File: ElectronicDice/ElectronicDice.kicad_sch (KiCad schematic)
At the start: 17 parts, among them J1 Conn_01x02_Pin, SW1 SW_Push

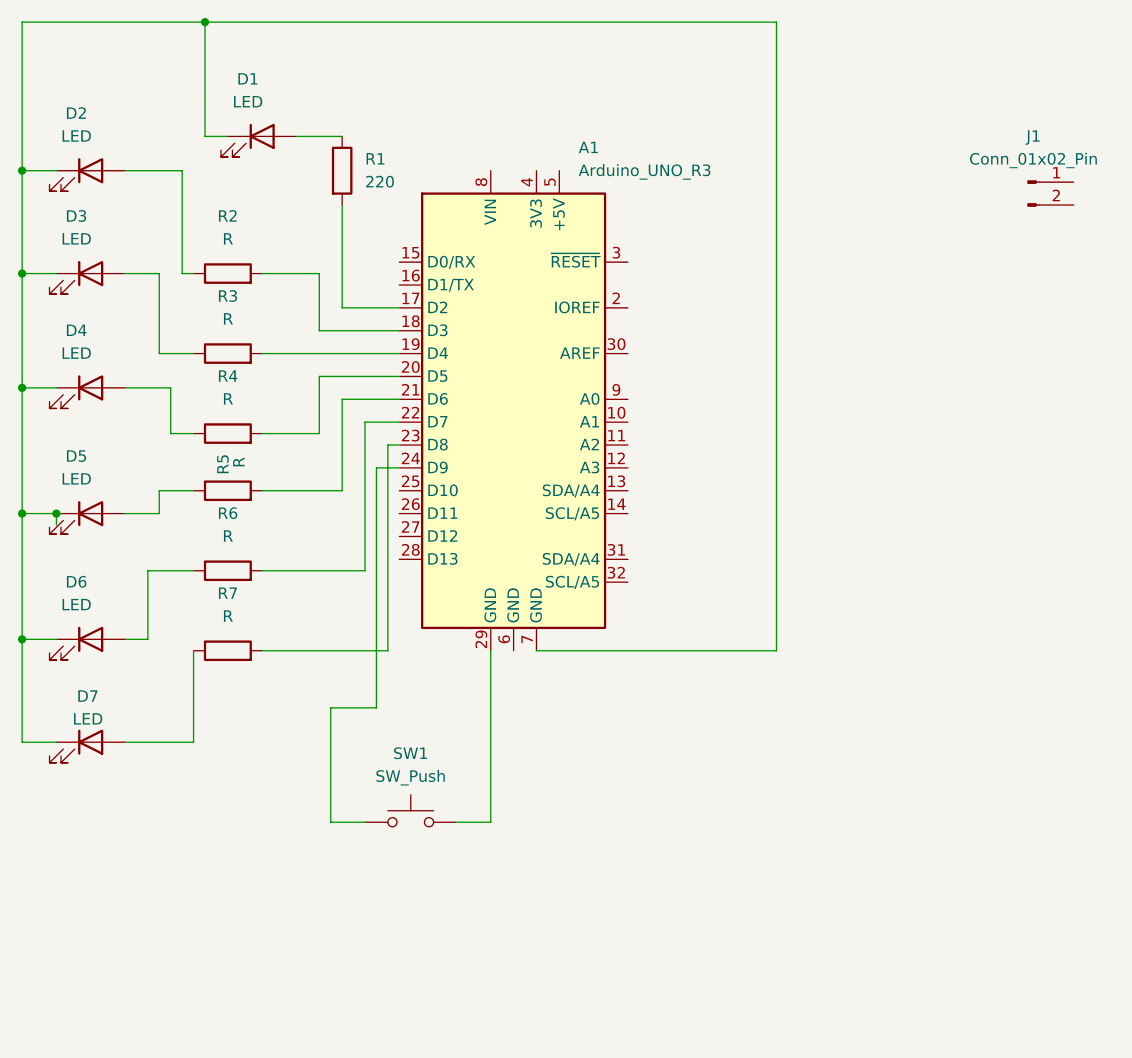
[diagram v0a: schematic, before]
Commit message: Assigned Footprints
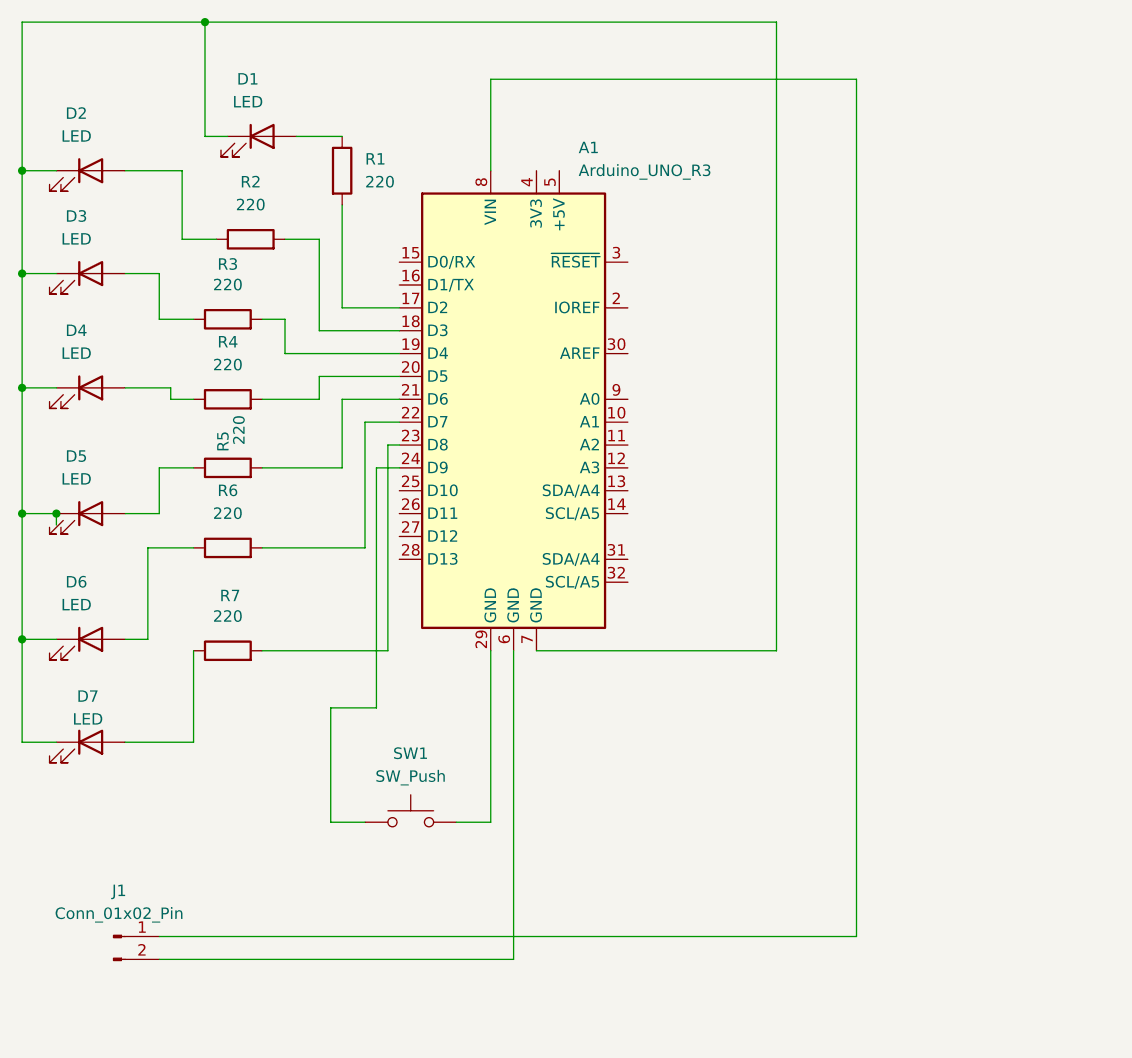
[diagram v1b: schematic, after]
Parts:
- D1, D2, D3, D4, D5, D6, D7: footprint (none) -> LED_THT:LED_D5.0mm
- J1: footprint (none) -> Connector_PinHeader_2.54mm:PinHeader_1x02_P2.54mm_Vertical
- R1: footprint (none) -> Resistor_THT:R_Axial_DIN0207_L6.3mm_D2.5mm_P10.16mm_Horizontal
- R2: value R -> 220; footprint (none) -> Resistor_THT:R_Axial_DIN0207_L6.3mm_D2.5mm_P10.16mm_Horizontal
- R3, R4, R5, R6, R7: value R -> 220; footprint (none) -> Resistor_THT:R_Axial_DIN0207_L6.3mm_D2.5mm_P15.24mm_Horizontal
- SW1: footprint (none) -> Button_Switch_THT:SW_PUSH_6mm
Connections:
- net at J1.1 (Pin_1): now also A1.8 (VIN)
- net at J1.2 (Pin_2): now also A1.6 (GND)
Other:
- moved on the sheet: J1, R2, R3, R4, R5, R6

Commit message: Ran ECR and fixed the errors with the circuit
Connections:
- net at A1.8 (VIN): no longer J1.1 (Pin_1)
- net GND: now reaches A1.6 (GND), J1.2 (Pin_2)
- net GND: now also A1.29 (GND), A1.7 (GND), D1.1 (K), D2.1 (K), D3.1 (K), D4.1 (K), D5.1 (K), D6.1 (K), D7.1 (K), SW1.2
- net +5V: now reaches A1.5 (+5V)
- net +5V: now also J1.1 (Pin_1)
- no-connect marks 0 -> 19

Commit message: Added connections in PCB
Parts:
- R3, R4, R5, R6, R7: footprint Resistor_THT:R_Axial_DIN0207_L6.3mm_D2.5mm_P15.24mm_Horizontal -> Resistor_THT:R_Axial_DIN0207_L6.3mm_D2.5mm_P10.16mm_Horizontal
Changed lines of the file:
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@@
 			)
 		)
-		(property "Footprint" "Resistor_THT:R_Axial_DIN0207_L6.3mm_D2.5mm_P15.24mm_Horizontal"
+		(property "Footprint" "Resistor_THT:R_Axial_DIN0207_L6.3mm_D2.5mm_P10.16mm_Horizontal"
 			(at 104.14 81.788 90)
 			(hide yes)
@@
 			)
 		)
-		(property "Footprint" "Resistor_THT:R_Axial_DIN0207_L6.3mm_D2.5mm_P15.24mm_Horizontal"
+		(property "Footprint" "Resistor_THT:R_Axial_DIN0207_L6.3mm_D2.5mm_P10.16mm_Horizontal"
 			(at 104.14 89.408 90)
 			(hide yes)
@@
 			)
 		)
-		(property "Footprint" "Resistor_THT:R_Axial_DIN0207_L6.3mm_D2.5mm_P15.24mm_Horizontal"
+		(property "Footprint" "Resistor_THT:R_Axial_DIN0207_L6.3mm_D2.5mm_P10.16mm_Horizontal"
 			(at 104.14 98.298 90)
 			(hide yes)
@@
 			)
 		)
-		(property "Footprint" "Resistor_THT:R_Axial_DIN0207_L6.3mm_D2.5mm_P15.24mm_Horizontal"
+		(property "Footprint" "Resistor_THT:R_Axial_DIN0207_L6.3mm_D2.5mm_P10.16mm_Horizontal"
 			(at 104.14 72.898 90)
 			(hide yes)
@@
 			)
 		)
-		(property "Footprint" "Resistor_THT:R_Axial_DIN0207_L6.3mm_D2.5mm_P15.24mm_Horizontal"
+		(property "Footprint" "Resistor_THT:R_Axial_DIN0207_L6.3mm_D2.5mm_P10.16mm_Horizontal"
 			(at 104.14 109.728 90)
 			(hide yes)
